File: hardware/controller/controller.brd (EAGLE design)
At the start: 168 x 70 mm, 62 parts, among them IC1 MAX3232ECD, IC3 NRF24L01P-R7, IC4 TPS562231DRLR, Q1 16M, Q3 FDN360P, U2 ATMEGA328P-AU, X1 RS232, Y1 8MHz

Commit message: lots of stuff
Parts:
- added C8: (no value), Wurth_Elektronik_Passive_Capacitors_rev18b:4.2X1.9X2.8(BXCXA)
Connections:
- net CE: now also U2.12; no longer U2.13
- net CSN: now also U2.13; no longer U2.14
- net GND: now also C8.2
- net S_LOCK: now also U2.10; no longer U2.12
- net S_POWER: now also U2.9; no longer U2.10
- net VCC: now also C8.1
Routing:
- net S_LOCK: track 58.2 -> 0.00 mm, vias 1 -> 0
- net S_UNLOCK: track 58.1 -> 0.00 mm, vias 1 -> 0
- net VCC: track 260.1 -> 268.0 mm
- net CSN: track 58.6 -> 57.3 mm
- net MISO: track 107.0 -> 105.7 mm
- net S_POWER: track 41.8 -> 40.7 mm
- net CE: track 59.7 -> 60.8 mm
- net MOSI: track 99.3 -> 99.9 mm
- net GND: vias 8 -> 9

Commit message: start remote
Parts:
- added B1, B2: (no value), Fidget Spinner Example:CR2032_SMT_BAT-HLD-001
- added C22: 0.1u, rcl:C0805
- added E2: ANTENNA-GROUNDEDTRACE-15.2MM, SparkFun-RF:TRACE_ANTENNA_2.4GHZ_15.2MM
- added J1: 43650-0500, 43650-0500:436500500
- added K1, K2: G5V1, relay:G5V1
- added LED1, LED2: (no value), led:CHIPLED_0805
- added Q2, Q4: FDN360P, transistor-power:SUPER-SOT3
- added R16, R18: 10k, rcl:R0805
- added R17, R19: 1k, rcl:R0805
- added R20: 1M, rcl:R0805
- added TP1, TP2, TP3: TPB1,27, testpad:B1,27
- added U1: ATMEGA328P-AU, Microcontroller:TQFP-32
- added Y2: 8MHz, SparkFun-Clocks:RESONATOR-SMD-3.2X1.3
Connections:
- new net E_LOCK: J1.1, K1.10
- new net E_UNLOCK: J1.3, K2.10
- new net GND1: B1.-, B2.-, C22.2, U1.21, U1.3, U1.5, Y2.2
- new net N$20: R20.2, U1.7, Y2.1
- new net N$29: J1.2, K1.5, K1.6, K2.5, K2.6
- new net N$32: R20.1, U1.8, Y2.3
- new net N$34: K1.2, Q2.3
- new net N$35: K2.2, Q4.3
- new net N$36: C22.1, U1.20
- new net N$37: LED1.A, R17.2
- new net N$39: LED2.A, R19.1
- new net VCC/2: B1.+$1, B1.+$2, B2.+$1, B2.+$2, U1.18, U1.4, U1.6
- net BAT: now also J1.5, Q2.2, Q4.2, TP1.TP
- net GND: now also J1.4, K1.9, K2.9, LED1.C, LED2.C, R16.2, R18.1, TP2.TP
- net S_LOCK: now also Q2.1, R18.2, R19.2
- net S_UNLOCK: now also Q4.1, R16.1, R17.1
- net VCC: now also TP3.TP
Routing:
- net BAT: track 6.68 -> 128.7 mm
- net S_LOCK: track 0.00 -> 116.6 mm, vias 0 -> 2
- net S_UNLOCK: track 0.00 -> 106.6 mm, vias 0 -> 2
- net N$29: track 0.00 -> 36.9 mm
- net E_LOCK: track 0.00 -> 29.5 mm
- net E_UNLOCK: track 0.00 -> 13.6 mm
- net N$34: track 0.00 -> 12.6 mm
- net N$35: track 0.00 -> 12.6 mm
- net N$39: track 0.00 -> 3.16 mm
- net N$37: track 0.00 -> 3.16 mm
- net VCC: track 268.0 -> 270.4 mm
- net GND: vias 9 -> 10
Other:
- board text added: "BAT"
- board text added: "VCC"

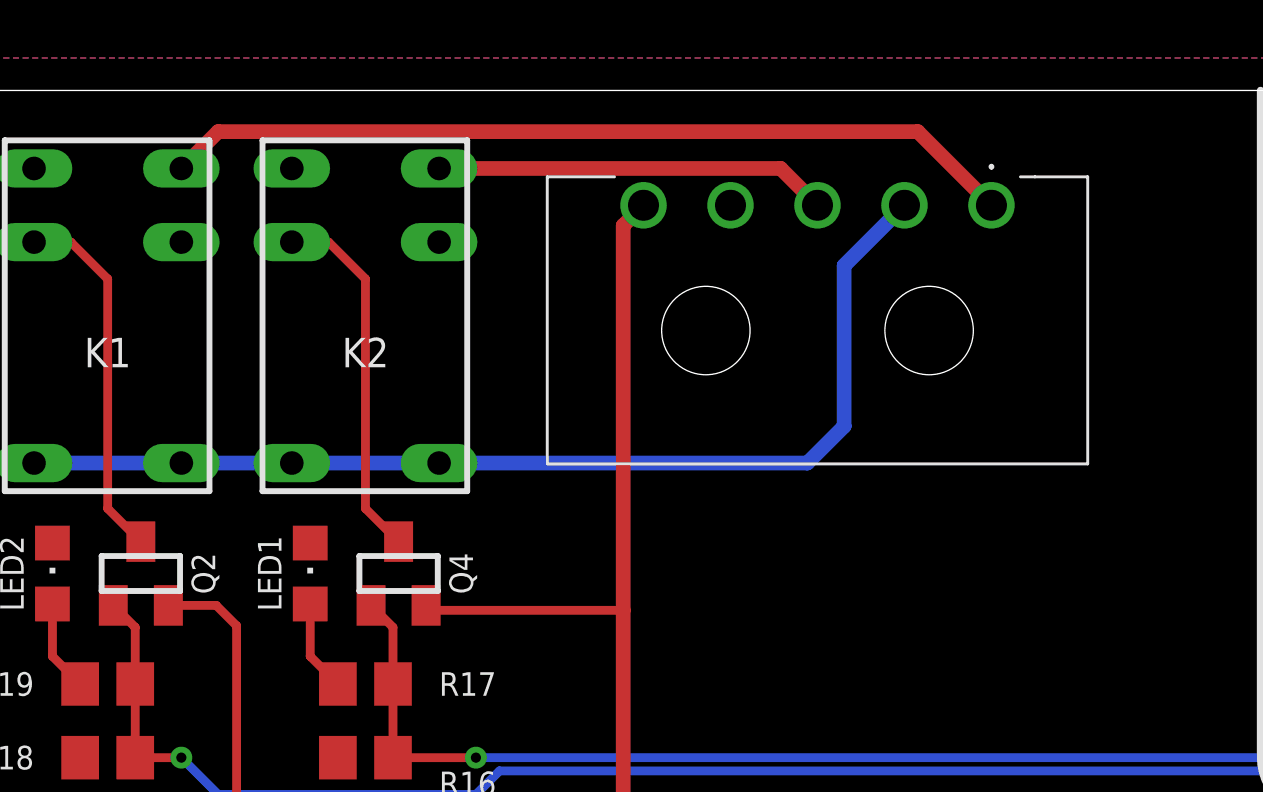
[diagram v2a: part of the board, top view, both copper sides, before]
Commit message: use 3x2 instead of 5x1
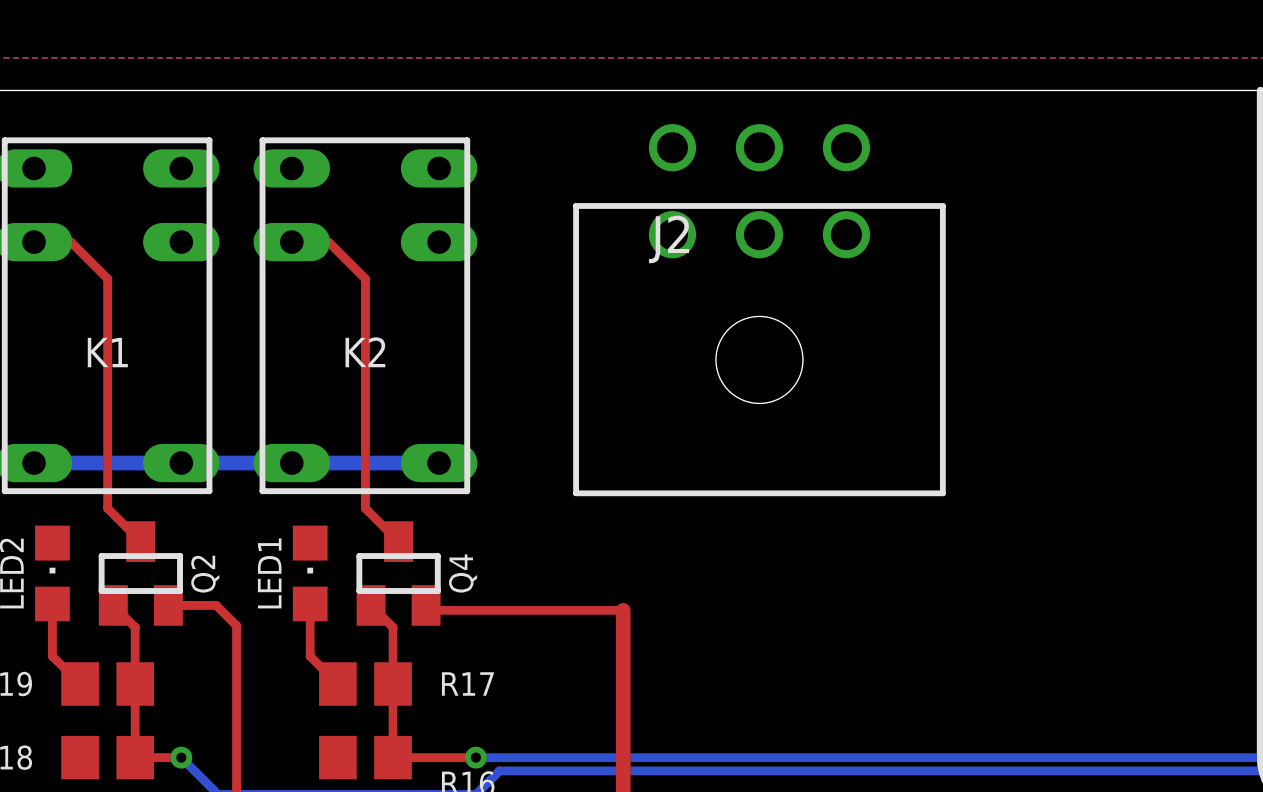
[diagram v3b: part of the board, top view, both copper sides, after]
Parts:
- removed J1: 43650-0500, 43650-0500:436500500
- added J2: 43045-0600, 43045-0600:43045-0600
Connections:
- net BAT: now also J2.1; no longer J1.5
- net E_LOCK: no longer J1.1
- net E_UNLOCK: no longer J1.3
- net GND: no longer J1.4
- net N$29: no longer J1.2
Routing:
- net E_LOCK: track 29.5 -> 0.00 mm
- net N$29: track 36.9 -> 14.0 mm
- net BAT: track 128.7 -> 114.5 mm
- net E_UNLOCK: track 13.6 -> 0.00 mm
